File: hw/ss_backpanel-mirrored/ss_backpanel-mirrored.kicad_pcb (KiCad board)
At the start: 2 copper layers, 165 x 51.1 mm, 18 parts, among them J101 4mm_banana_socket-LB_I4R_A-pa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, M101 Amphenol_T3437000-DIN7_panel_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, M102 Amphenol_T3437000-DIN7_panel_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, M103 Schurter-3101_0060-fuse_holde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, M104 FN283-1-06_Schaffner_AC-panel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, M105 74980104400-Wurth_RJ45-Panel_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, M106 TE-1734346-Panel_cutout, M107 CUI-UJ2_AH_1_SMT-Panel_cutout, M108 DSub9-Kycon_K22X-E9P-N-panel_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, M109 SJ-3571N_CUI_audio_jacket_pan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, M110 SMA_bulkhead_jack_Panel_cutout, M111 Molex_NanoFit-1x02-Panel_cuto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

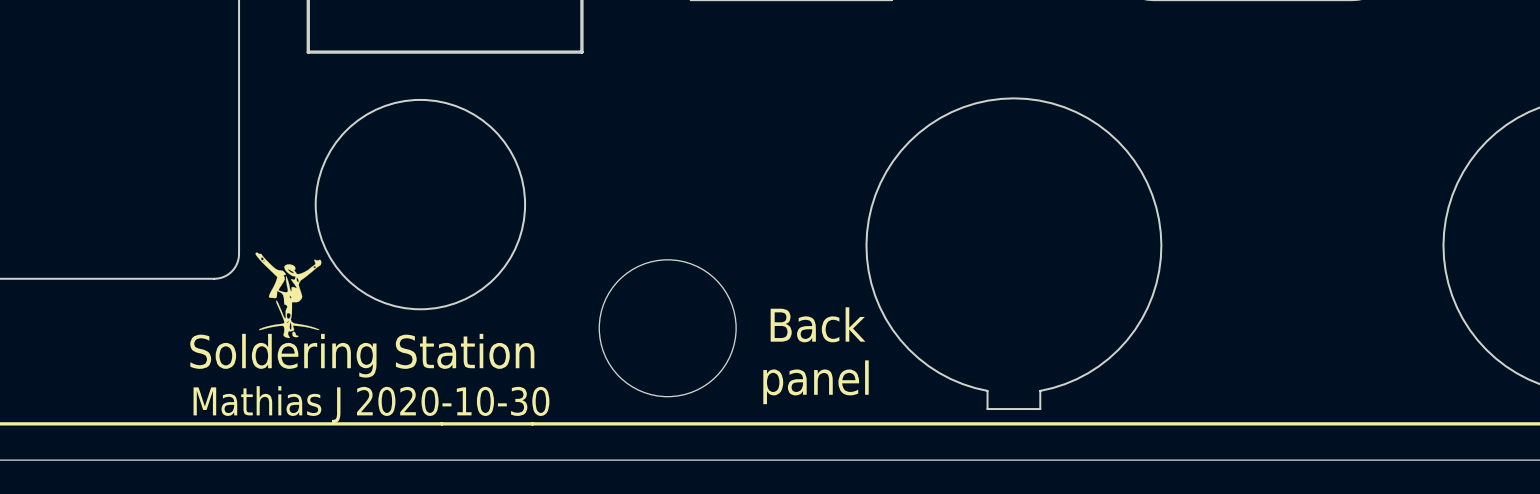
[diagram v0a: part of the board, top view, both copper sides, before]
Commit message: New mech main-track selected: "centered PSU" + "Mirrored back panel". Minor cleanups & re-alignments.
(Yet ToDo: all MB adjustments...)
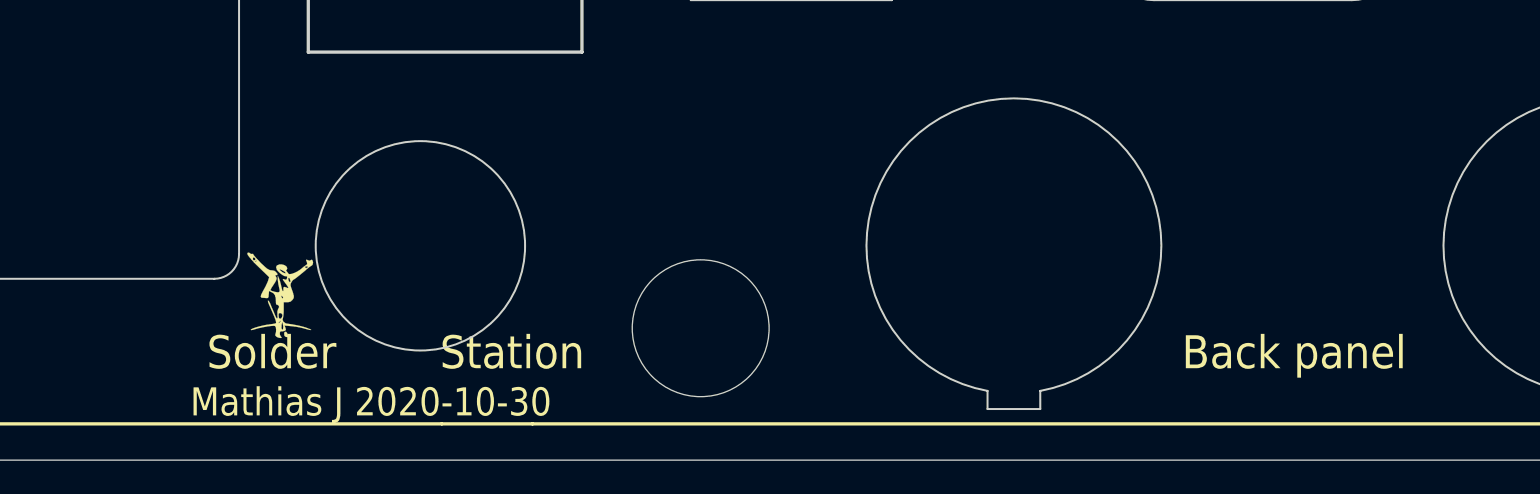
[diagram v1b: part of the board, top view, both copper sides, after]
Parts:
- moved M103 2.50 mm to (146.0, 87.0)
- moved J101 2.00 mm to (163.0, 92.0)
- moved Logo103 0.50 mm to (137.5, 90.0)
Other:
- board text added: "Solder Station"
- board text removed: "Soldering Station"

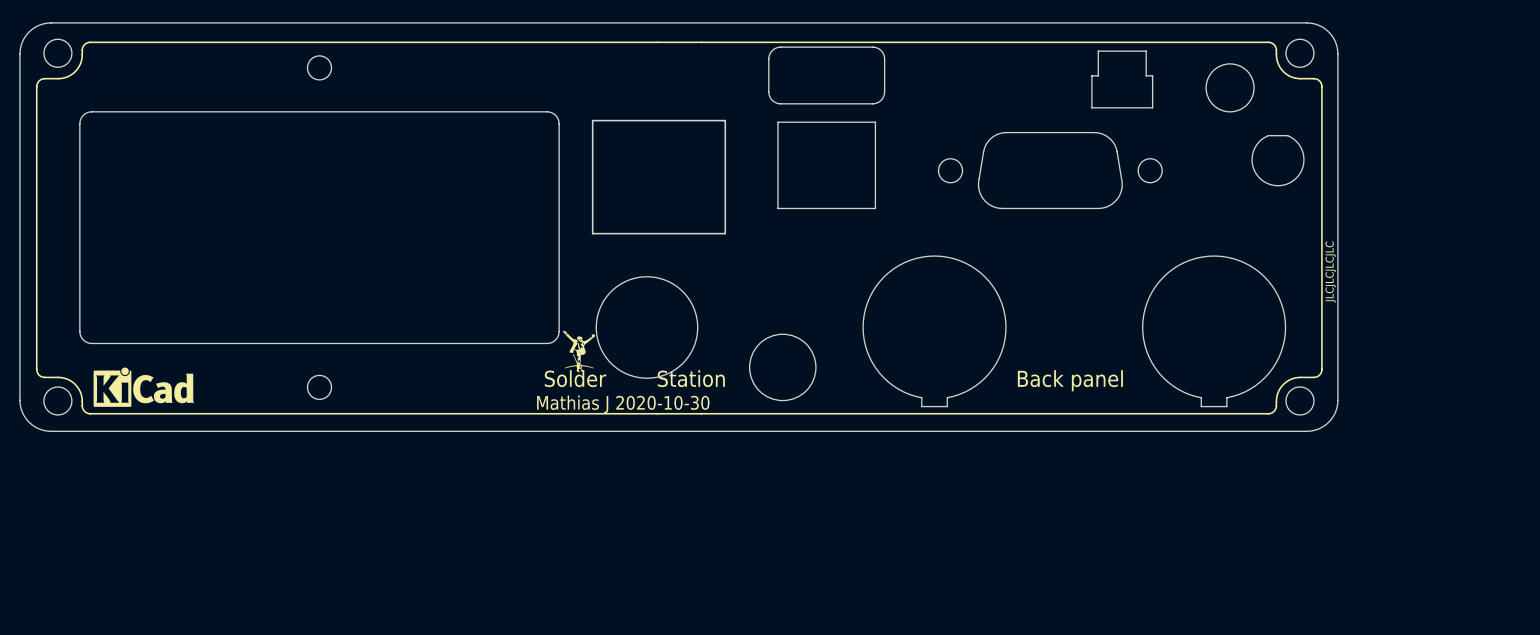
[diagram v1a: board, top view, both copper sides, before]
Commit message: Minor re-alignments of rear-panel items that collided with box sides (SMA, outer DIN, Schaffner AC-in)
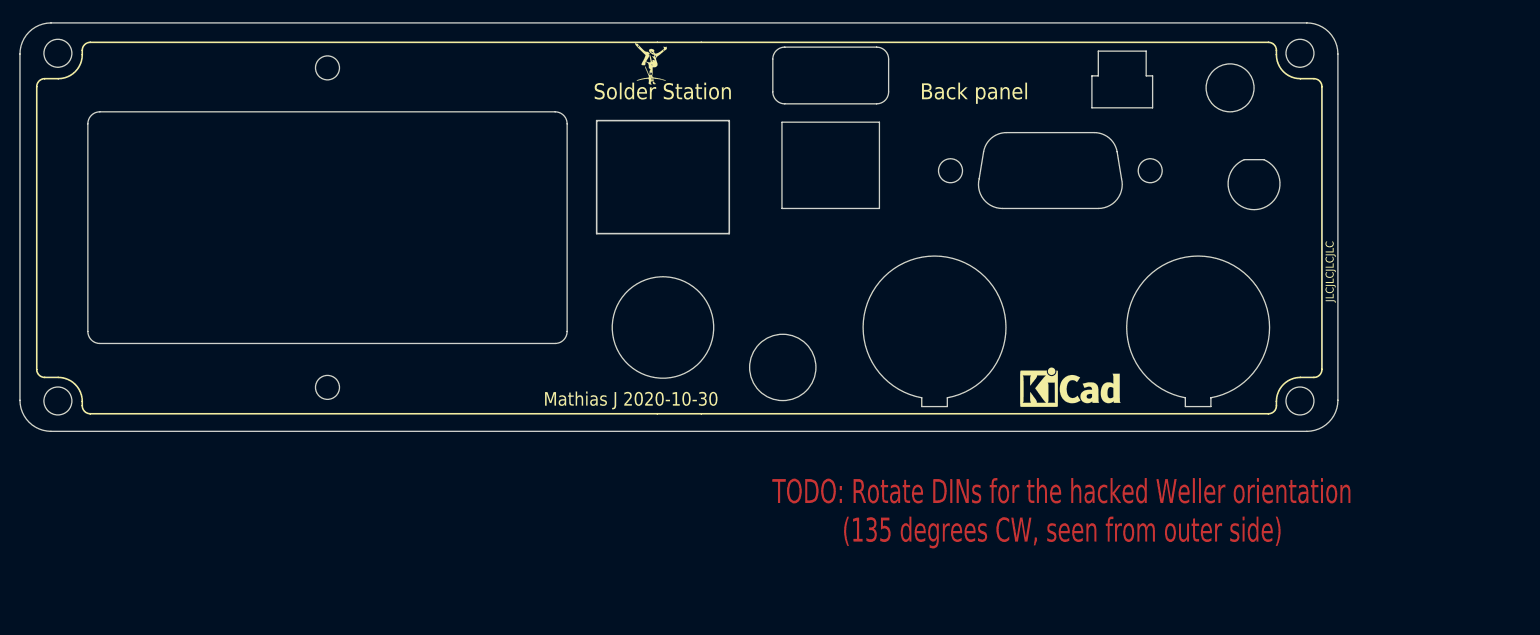
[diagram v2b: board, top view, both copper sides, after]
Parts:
- moved LOGO101 116.0 mm to (199.0, 95.0)
- moved Logo103 37.1 mm to (146.5, 54.0)
- moved M110 4.24 mm to (222.0, 69.0)
- moved M101 2.00 mm to (215.0, 87.0)
- moved M103 2.00 mm to (148.0, 87.0)
- moved M104 1.00 mm to (106.0, 74.5)
- moved M105 0.50 mm to (148.0, 61.1)
- moved M106 0.50 mm to (169.0, 61.1)
- moved M107 0.50 mm to (169.0, 59.5)
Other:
- board text added: "TODO: Rotate DINs for the hacked Weller orientation (135 degrees CW, seen from outer side)"

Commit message: Rearpanel: IDC 2x5 instead of Dsub9 as dbg/bootstrp conn. Remove secondary fuseholder; rearrange DIN, P.E. banana, dbg. for more space. MainBoard: Rotate MW PSU 180deg (optimize for 230V through PwrBtn). PCB-fuse for 12V secondary side. IDC 2x5 instead of Dsub9; include DbgLED on free pin; ESD TVS on all dbgcon pins
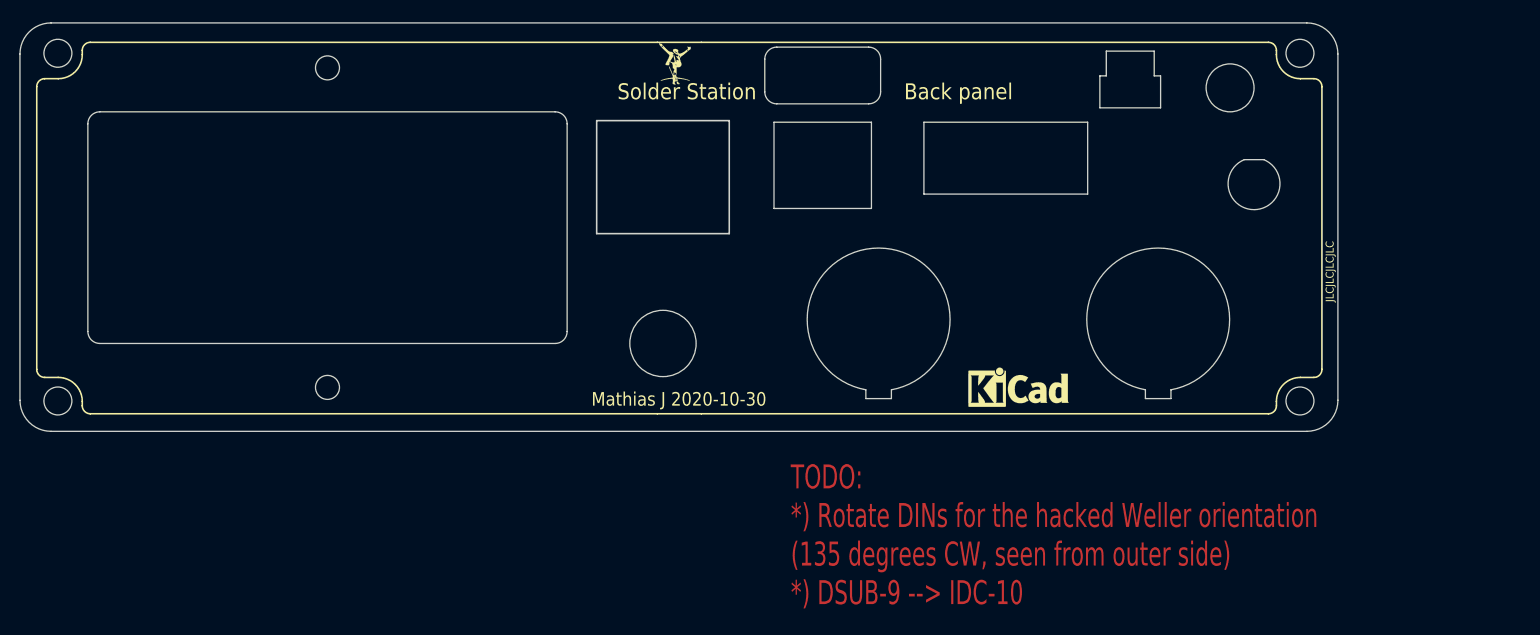
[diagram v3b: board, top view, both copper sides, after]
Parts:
- removed M108: DSub9-Kycon_K22X-E9P-N-panel_cutout-small, customlib_mj_fp:DSub9-Kycon_K22X-E9P-N_panel_cutout_behind
- M103: value Schurter-3101_0060-fuse_holder-Panel_cutout -> Mech_cutout_IDC_2x5; footprint customlib_mj_fp:Schurter_3101_0060_fuse_holder-panel_cutout -> customlib_mj_fp:Mech_cutout_IDC_2x5
- moved M103 50.0 mm to (190.9, 61.3), turned to 180 degrees
- moved J101 15.3 mm to (148.0, 89.0)
- moved M102 7.07 mm to (175.0, 86.0)
- moved LOGO101 6.50 mm to (192.5, 95.0)
- moved M101 5.10 mm to (210.0, 86.0)
- moved Logo103 3.00 mm to (149.5, 54.0)
- moved M106 1.00 mm to (168.0, 61.1)
- moved M107 1.00 mm to (168.0, 59.5)
- moved M111 1.00 mm to (206.5, 59.5)
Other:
- board text added: "TODO: *) Rotate DINs for the hacked Weller orientation (135 degrees CW, seen from outer side) *) DSUB-9 --> IDC-10"
- board text removed: "TODO: Rotate DINs for the hacked Weller orientation (135 degrees CW, seen from outer side)"
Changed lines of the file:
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@@
     (tracks 0)
     (zones 0)
-    (modules 18)
+    (modules 17)
     (nets 1)
   )
@@
     (uvia_drill 0.1)
   )
+  (module customlib_mj_fp:Mech_cutout_IDC_2x5 locked (layer F.Cu)
+    (at 190.92 61.3 180)
+    (descr "Panel cut-out for a right-angled IDC 2x5")
+    (tags "IDC 2x5")
+    (attr virtual)
+    (fp_text reference M103 (at 0 -7.5) (layer F.Fab)
+      (effects (font (size 1.2 0.8) (thickness 0.16)))
+    )
+    (fp_text value Mech_cutout_IDC_2x5 (at 0 -0.6) (layer F.Fab)
+      (effects (font (size 1 1) (thickness 0.15)))
+    )
+    (fp_line (start -10.25 -9) (end 10.25 -9) (layer F.CrtYd) (width 0.12))
+    (fp_line (start -10.25 0) (end 10.25 0) (layer F.CrtYd) (width 0.12))
+    (fp_line (start -10.25 -9) (end -10.25 0) (layer F.CrtYd) (width 0.12))
+    (fp_line (start 10.25 -9) (end 10.25 0) (layer F.CrtYd) (width 0.12))
+    (fp_line (start -10.25 -9) (end 10.25 -9) (layer Edge.Cuts) (width 0.12))
+    (fp_line (start -10.25 0) (end 10.25 0) (layer Edge.Cuts) (width 0.12))
+    (fp_line (start -10.25 -9) (end -10.25 0) (layer Edge.Cuts) (width 0.12))
+    (fp_line (start 10.25 -9) (end 10.25 0) (layer Edge.Cuts) (width 0.12))
+    (model ${KISYS3DMOD}/Connector_IDC.3dshapes/IDC-Header_2x05_P2.54mm_Horizontal.step
+      (offset (xyz -5.08 0 11.5))
+      (scale (xyz 1 1 1))
+      (rotate (xyz 0 -90 -90))
+    )
+  )
   (module customlib_mj_fp:Molex_NanoFit-1x02-Panel_cutout locked (layer B.Cu)
-    (at 205.5 59.5 180)
+    (at 206.5 59.5 180)
     (descr "Panel cut-out for Molex Nano-Fit 1x02")
     (tags "Molex NanoFit panel cut-out")
@@
     )
   )
-  (module customlib_mj_fp:DSub9-Kycon_K22X-E9P-N_panel_cutout_behind locked (layer B.Cu)
-    (at 196.5 61.1)
-    (descr "Dsub-9 panel cut-out, behind")
-    (tags "DSUB-9 panel cut-out")
-    (attr virtual)
-    (fp_text reference M108 (at 0 6.5) (layer B.Fab)
-      (effects (font (size 1.2 0.8) (thickness 0.16)) (justify mirror))
-    )
-    (fp_text value DSub9-Kycon_K22X-E9P-N-panel_cutout-small (at 0 2.5) (layer B.Fab)
-      (effects (font (size 1 1) (thickness 0.15)) (justify mirror))
-    )
-    (fp_line (start -8.910887 7.274234) (end -8.355942 3.89642) (layer Edge.Cuts) (width 0.12))
-    (fp_line (start 6 11) (end -6 11) (layer Edge.Cuts) (width 0.12))
-    (fp_line (start 8.355942 3.89642) (end 8.910887 7.274234) (layer Edge.Cuts) (width 0.12))
-    (fp_line (start -5.5 1.5) (end 5.5 1.5) (layer Edge.Cuts) (width 0.12))
-    (fp_line (start -8.910887 7.274234) (end -8.355942 3.89642) (layer Dwgs.User) (width 0.12))
-    (fp_line (start 6 11) (end -6 11) (layer Dwgs.User) (width 0.12))
-    (fp_line (start 8.355942 3.89642) (end 8.910887 7.274234) (layer Dwgs.User) (width 0.12))
-    (fp_line (start -5.5 1.5) (end 5.5 1.5) (layer Dwgs.User) (width 0.12))
-    (fp_arc (start -5.5 4.4) (end -8.355942 3.89642) (angle 80) (layer Dwgs.User) (width 0.12))
-    (fp_arc (start 6 8) (end 8.910887 7.274234) (angle 104) (layer Dwgs.User) (width 0.12))
-    (fp_arc (start -6 8) (end -6 11) (angle 104) (layer Dwgs.User) (width 0.12))
-    (fp_arc (start 5.5 4.4) (end 5.5 1.5) (angle 80) (layer Dwgs.User) (width 0.12))
-    (fp_arc (start 5.5 4.4) (end 5.5 1.5) (angle 80) (layer Edge.Cuts) (width 0.12))
-    (fp_arc (start -5.5 4.4) (end -8.355942 3.89642) (angle 80) (layer Edge.Cuts) (width 0.12))
-    (fp_arc (start 6 8) (end 8.910887 7.274234) (angle 104) (layer Edge.Cuts) (width 0.12))
-    (fp_arc (start -6 8) (end -6 11) (angle 104) (layer Edge.Cuts) (width 0.12))
-    (pad "" np_thru_hole circle (at 12.5 6.275) (size 3 3) (drill 3) (layers *.Cu *.Mask))
-    (pad "" np_thru_hole circle (at -12.5 6.275) (size 3 3) (drill 3) (layers *.Cu *.Mask))
-    (model /home/mjoh/projects/stm32/projects/customlib_mj/3d_models/K22X-E9P-N.step
-      (offset (xyz 0 6.275 -2.5))
-      (scale (xyz 1 1 1))
-      (rotate (xyz 0 0 0))
-    )
-  )
   (module customlib_mj_fp:SMA_Bulkhead_jack-Panel_cutout (layer B.Cu)
     (at 222 69 90)
@@
   )
   (module customlib_mj_fp:LB_I4R_A-4mm_banana_socket_panelmnt locked (layer B.Cu)
-    (at 163 92 180)
+    (at 148 89 180)
     (fp_text reference J101 (at 0 5) (layer B.SilkS) hide
       (effects (font (size 1.2 0.8) (thickness 0.16)) (justify mirror))
@@
   )
   (module customlib_mj_fp:CUI-UJ2_AH_1_SMT-Panel_cutout locked (layer B.Cu)
-    (at 169 59.5 180)
+    (at 168 59.5 180)
     (descr "Panel cut-out for CUI-UJ2_AH_1_SMT USB-A host connector")
     (tags "USB-A CUI UJ2_AH_1_SMT panel cut-out")
@@
   )
   (module customlib_mj_fp:TE_1734346-Panel_cutout locked (layer B.Cu)
-    (at 169 61.1)
+    (at 168 61.1)
     (descr "Panel cut-out for TE-1734346 USB-B device connector")
     (tags "USB-B TE-1734346 panel cut-out")
@@
     )
   )
-  (module customlib_mj_fp:Schurter_3101_0060_fuse_holder-panel_cutout locked (layer F.Cu)
-    (at 148 87)
-    (fp_text reference M103 (at 0 0.6) (layer F.Fab)
-      (effects (font (size 1.2 0.8) (thickness 0.16)))
-    )
-    (fp_text value Schurter-3101_0060-fuse_holder-Panel_cutout (at 0 7) (layer F.Fab)
-      (effects (font (size 1 1) (thickness 0.15)))
-    )
-    (fp_circle (center 0 0) (end 6.35 0) (layer Dwgs.User) (width 0.12))
-    (fp_circle (center 0 0) (end 6.35 0) (layer Edge.Cuts) (width 0.12))
-    (model /home/mjoh/projects/stm32/projects/SolderingStation/mech/Schurter-0031.0060_002-fuseholder.stp
-      (offset (xyz 0 0 -8.800000000000001))
-      (scale (xyz 1 1 1))
-      (rotate (xyz 0 0 -90))
-    )
-  )
   (module customlib_mj_fp:Amphenol_T3437000-DIN7-panel_cutout locked (layer B.Cu)
-    (at 182 87 180)
+    (at 175 86 180)
     (descr "Amphenol T3437000 DIN7 (Weller connector) panel cutout")
     (tags "Amphenol T3437000 DIN7 panel cutout")
@@
   )
   (module customlib_mj_fp:Amphenol_T3437000-DIN7-panel_cutout locked (layer B.Cu)
-    (at 215 87 180)
+    (at 210 86 180)
     (descr "Amphenol T3437000 DIN7 (Weller connector) panel cutout")
     (tags "Amphenol T3437000 DIN7 panel cutout")
@@
   )
   (module Symbol:KiCad-Logo_5mm_SilkScreen (layer F.Cu)
-    (at 199 95)
+    (at 192.5 95)
     (descr "KiCad Logo")
     (tags "Logo KiCad")
@@
   )
   (module customlib_mj_fp:MJ_Mini (layer F.Cu)
-    (at 146.5 54)
+    (at 149.5 54)
     (tags "MJ mini")
     (fp_text reference Logo103 (at 0 3.8) (layer F.SilkS) hide
@@
       (xy -1.83067 -2.546882)) (layer F.SilkS) (width 0.01))
   )
-  (gr_text "TODO: Rotate DINs for the hacked Weller orientation\n(135 degrees CW, seen from outer side)" (at 198 110) (layer F.Cu)
-    (effects (font (size 3 2) (thickness 0.5)))
-  )
-  (gr_text "Back panel" (at 187 57.5) (layer F.SilkS)
+  (gr_text "TODO: \n*) Rotate DINs for the hacked Weller orientation\n(135 degrees CW, seen from outer side)\n*) DSUB-9 --> IDC-10" (at 164 113) (layer F.Cu)
+    (effects (font (size 3 2) (thickness 0.5)) (justify left))
+  )
+  (gr_text "Back panel" (at 185 57.5) (layer F.SilkS)
     (effects (font (size 2 1.8) (thickness 0.4)))
   )
@@
   (gr_line (start 70 59.5) (end 230 59.5) (layer Dwgs.User) (width 0.15))
   (gr_line (start 230 61.1) (end 70 61.1) (layer Dwgs.User) (width 0.15))
-  (gr_text "Solder Station" (at 148 57.5) (layer F.SilkS)
+  (gr_text "Solder Station" (at 151 57.5) (layer F.SilkS)
     (effects (font (size 2 1.8) (thickness 0.4)))
   )
-  (gr_text "Mathias J 2020-10-30" (at 144 96) (layer F.SilkS)
+  (gr_text "Mathias J 2020-10-30" (at 150 96) (layer F.SilkS)
     (effects (font (size 1.7 1.5) (thickness 0.3)))
   )
